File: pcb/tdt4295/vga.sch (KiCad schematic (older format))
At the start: 33 parts

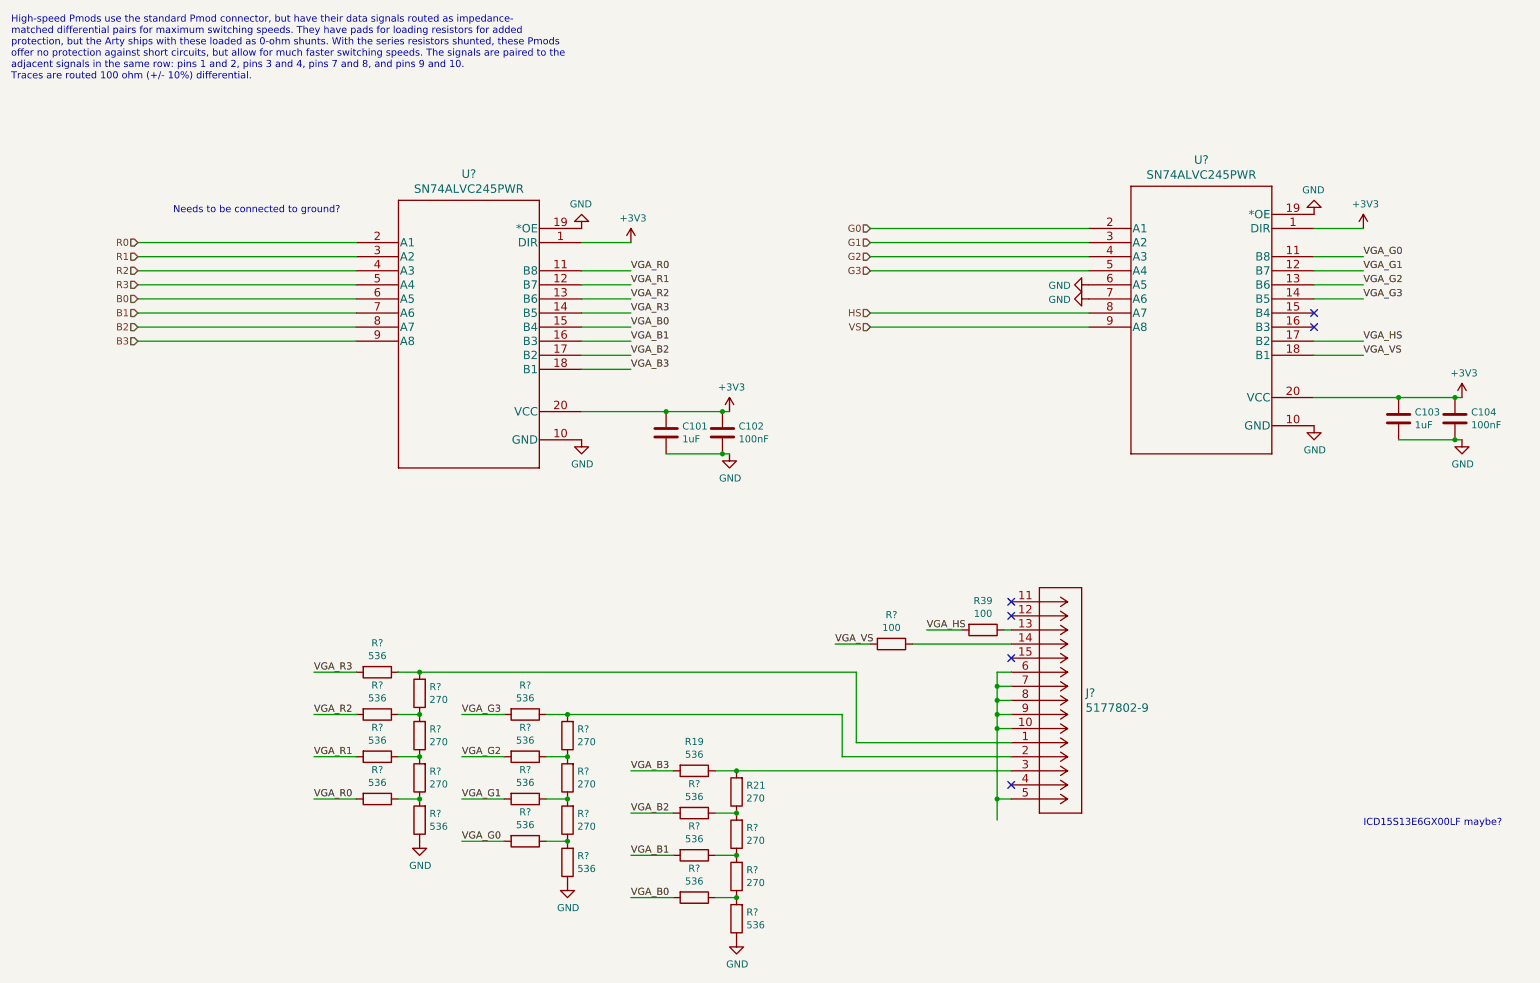
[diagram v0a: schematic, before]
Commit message: fpga external pin headers
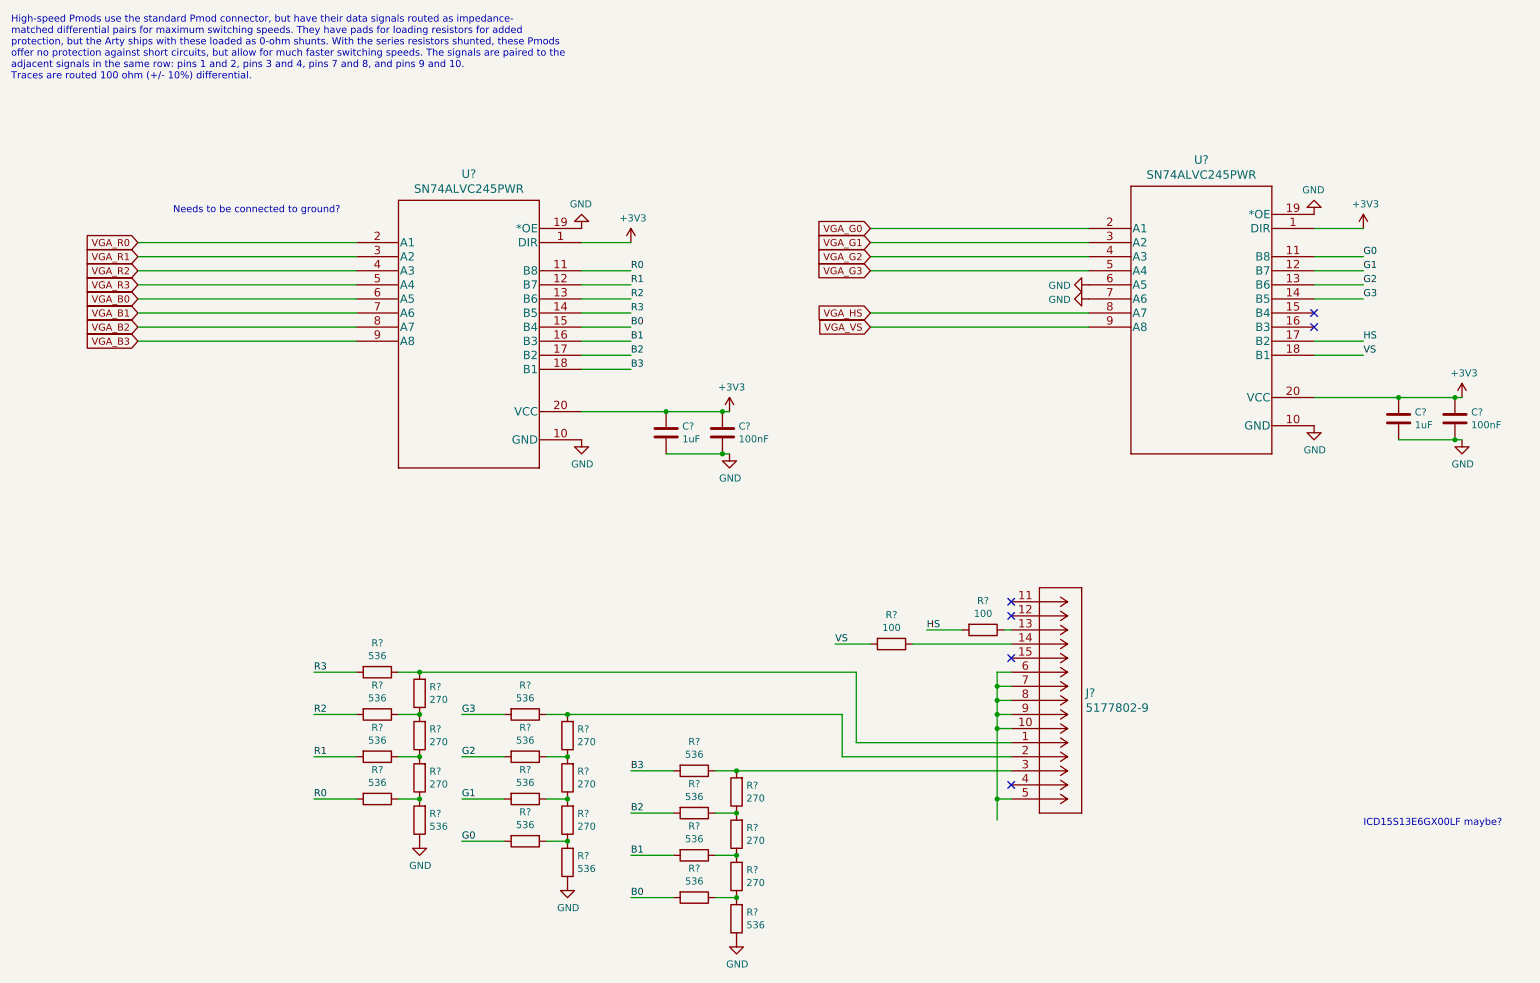
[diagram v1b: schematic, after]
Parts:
- renumbered C101 to C?, C102 to C?, C103 to C?, C104 to C?, R39 to R?, R19 to R?, R21 to R?
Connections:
- net B0: now also R?.2, U?.15 (B4); no longer U?.6 (A5)
- net B1: now also R?.2, U?.16 (B3); no longer U?.7 (A6)
- net B2: now also R?.2, U?.17 (B2); no longer U?.8 (A7)
- net B3: now also R?.2, U?.18 (B1); no longer U?.9 (A8)
- net G0: now also R?.2, U?.11 (B8); no longer U?.2 (A1)
- net G1: now also R?.2, U?.12 (B7); no longer U?.3 (A2)
- net G2: now also R?.2, U?.13 (B6); no longer U?.4 (A3)
- net G3: now also R?.2, U?.14 (B5); no longer U?.5 (A4)
- net HS: now also R?.2, U?.17 (B2); no longer U?.8 (A7)
- net R0: now also R?.2, U?.11 (B8); no longer U?.2 (A1)
- net R1: now also R?.2, U?.12 (B7); no longer U?.3 (A2)
- net R2: now also R?.2, U?.13 (B6); no longer U?.4 (A3)
- net R3: now also R?.2, U?.14 (B5); no longer U?.5 (A4)
- net VGA_B0: now also U?.6 (A5); no longer R?.2, U?.15 (B4)
- net VGA_B1: now also U?.7 (A6); no longer R?.2, U?.16 (B3)
- net VGA_B2: now also U?.8 (A7); no longer R?.2, U?.17 (B2)
- net VGA_B3: now also U?.9 (A8); no longer R?.2, U?.18 (B1)
- net VGA_G0: now also U?.2 (A1); no longer R?.2, U?.11 (B8)
- net VGA_G1: now also U?.3 (A2); no longer R?.2, U?.12 (B7)
- net VGA_G2: now also U?.4 (A3); no longer R?.2, U?.13 (B6)
- net VGA_G3: now also U?.5 (A4); no longer R?.2, U?.14 (B5)
- net VGA_HS: now also U?.8 (A7); no longer R?.2, U?.17 (B2)
- net VGA_R0: now also U?.2 (A1); no longer R?.2, U?.11 (B8)
- net VGA_R1: now also U?.3 (A2); no longer R?.2, U?.12 (B7)
- net VGA_R2: now also U?.4 (A3); no longer R?.2, U?.13 (B6)
- net VGA_R3: now also U?.5 (A4); no longer R?.2, U?.14 (B5)
- net VGA_VS: now also U?.9 (A8); no longer R?.2, U?.18 (B1)
- net VS: now also R?.2, U?.18 (B1); no longer U?.9 (A8)
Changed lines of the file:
@@
 $Descr A4 11693 8268
 encoding utf-8
-Sheet 3 3
+Sheet 4 5
 Title ""
 Date ""
@@
 	4650 3350 5250 3350
 $Comp
-L Device:C C101
+L Device:C C?
 U 1 1 61467E30
 P 5250 3500
-F 0 "C101" H 5365 3546 50  0000 L CNN
+F 0 "C?" H 5365 3546 50  0000 L CNN
 F 1 "1uF" H 5365 3455 50  0000 L CNN
 F 2 "" H 5288 3350 50  0001 C CNN
@@
 Connection ~ 5250 3350
 $Comp
-L Device:C C102
+L Device:C C?
 U 1 1 614688C2
 P 5650 3500
-F 0 "C102" H 5765 3546 50  0000 L CNN
+F 0 "C?" H 5765 3546 50  0000 L CNN
 F 1 "100nF" H 5765 3455 50  0000 L CNN
 F 2 "" H 5688 3350 50  0001 C CNN
@@
 	5250 3350 5650 3350
 Text Label 5000 2350 0    50   ~ 0
-VGA_R0
+R0
 Text Label 5000 2450 0    50   ~ 0
-VGA_R1
-Text Label 5000 2550 0    50   ~ 0
-VGA_R2
-Text Label 5000 2650 0    50   ~ 0
-VGA_R3
+R1
 Text Label 5000 2750 0    50   ~ 0
-VGA_B0
+B0
 Text Label 5000 2850 0    50   ~ 0
-VGA_B1
+B1
 Text Label 5000 2950 0    50   ~ 0
-VGA_B2
+B2
 Text Label 5000 3050 0    50   ~ 0
-VGA_B3
+B3
 Wire Wire Line
 	3050 2250 1500 2250
@@
 Wire Wire Line
 	3050 2850 1500 2850
-Text HLabel 1500 2850 0    50   Input ~ 0
-B3
-Text HLabel 1500 2750 0    50   Input ~ 0
-B2
-Text HLabel 1500 2650 0    50   Input ~ 0
-B1
-Text HLabel 1500 2550 0    50   Input ~ 0
-B0
-Text HLabel 1500 2450 0    50   Input ~ 0
-R3
-Text HLabel 1500 2350 0    50   Input ~ 0
-R2
-Text HLabel 1500 2250 0    50   Input ~ 0
-R1
-Text HLabel 1500 2150 0    50   Input ~ 0
-R0
 Text Notes 1750 1950 0    50   ~ 0
 Needs to be connected to ground?\n
@@
 	9850 3250 10450 3250
 $Comp
-L Device:C C103
+L Device:C C?
 U 1 1 61478F90
 P 10450 3400
-F 0 "C103" H 10565 3446 50  0000 L CNN
+F 0 "C?" H 10565 3446 50  0000 L CNN
 F 1 "1uF" H 10565 3355 50  0000 L CNN
 F 2 "" H 10488 3250 50  0001 C CNN
@@
 Connection ~ 10450 3250
 $Comp
-L Device:C C104
+L Device:C C?
 U 1 1 61478F97
 P 10850 3400
-F 0 "C104" H 10965 3446 50  0000 L CNN
+F 0 "C?" H 10965 3446 50  0000 L CNN
 F 1 "100nF" H 10965 3355 50  0000 L CNN
 F 2 "" H 10888 3250 50  0001 C CNN
@@
 	9850 2950 10200 2950
 Text Label 10200 2250 0    50   ~ 0
-VGA_G0
+G0
 Text Label 10200 2350 0    50   ~ 0
-VGA_G1
+G1
 Text Label 10200 2450 0    50   ~ 0
-VGA_G2
+G2
 Text Label 10200 2550 0    50   ~ 0
-VGA_G3
+G3
 Text Label 10200 2850 0    50   ~ 0
-VGA_HS
+HS
 Text Label 10200 2950 0    50   ~ 0
-VGA_VS
+VS
 NoConn ~ 9850 2650
 NoConn ~ 9850 2750
@@
 Wire Wire Line
 	8250 2350 6700 2350
-Text HLabel 6700 2350 0    50   Input ~ 0
-G3
-Text HLabel 6700 2250 0    50   Input ~ 0
-G2
-Text HLabel 6700 2150 0    50   Input ~ 0
-G1
-Text HLabel 6700 2050 0    50   Input ~ 0
-G0
 Wire Wire Line
 	8250 2650 6700 2650
 Wire Wire Line
 	8250 2750 6700 2750
-Text HLabel 6700 2750 0    50   Input ~ 0
-VS
-Text HLabel 6700 2650 0    50   Input ~ 0
-HS
 Text Notes 10200 6300 0    50   ~ 0
 ICD15S13E6GX00LF maybe?\n
@@
 	7700 4900 7650 4900
 Text Label 7100 4900 0    50   ~ 0
-VGA_HS
-$Comp
-L Device:R R39
+HS
+$Comp
+L Device:R R?
 U 1 1 6147C891
 P 7500 4900
-F 0 "R39" V 7293 4900 50  0000 C CNN
+F 0 "R?" V 7293 4900 50  0000 C CNN
 F 1 "100" V 7384 4900 50  0000 C CNN
 F 2 "" V 7430 4900 50  0001 C CNN
@@
 $EndComp
 Text Label 6450 5000 0    50   ~ 0
-VGA_VS
+VS
 Wire Wire Line
 	6450 5000 6700 5000
@@
 	7700 5900 5750 5900
 $Comp
-L Device:R R19
+L Device:R R?
 U 1 1 61490189
 P 5450 5900
-F 0 "R19" V 5243 5900 50  0000 C CNN
+F 0 "R?" V 5243 5900 50  0000 C CNN
 F 1 "536" V 5334 5900 50  0000 C CNN
 F 2 "" V 5380 5900 50  0001 C CNN
@@
 $EndComp
 $Comp
-L Device:R R21
+L Device:R R?
 U 1 1 61490B3B
 P 5750 6050
-F 0 "R21" H 5680 6004 50  0000 R CNN
+F 0 "R?" H 5680 6004 50  0000 R CNN
 F 1 "270" H 5680 6095 50  0000 R CNN
 F 2 "" V 5680 6050 50  0001 C CNN
@@
 	2750 6100 3050 6100
 Text Label 5000 5900 0    50   ~ 0
+B3
+Text Label 5000 6200 0    50   ~ 0
+B2
+Text Label 5000 6500 0    50   ~ 0
+B1
+Text Label 5000 6800 0    50   ~ 0
+B0
+Text Label 3800 6400 0    50   ~ 0
+G0
+Text Label 3800 6100 0    50   ~ 0
+G1
+Text Label 3800 5800 0    50   ~ 0
+G2
+Text Label 3800 5500 0    50   ~ 0
+G3
+Text Label 2750 6100 0    50   ~ 0
+R0
+Text Label 2750 5800 0    50   ~ 0
+R1
+Text Label 2750 5500 0    50   ~ 0
+R2
+Text Label 2750 5200 0    50   ~ 0
+R3
+Wire Wire Line
+	7700 5800 6500 5800
+Wire Wire Line
+	6500 5800 6500 5500
+Wire Wire Line
+	7700 5700 6600 5700
+Wire Wire Line
+	6600 5700 6600 5200
+Wire Wire Line
+	3500 5200 6600 5200
+Text Label 5000 2550 0    50   ~ 0
+R2
+Text Label 5000 2650 0    50   ~ 0
+R3
+Text GLabel 1500 2150 0    50   Input ~ 0
+VGA_R0
+Text GLabel 1500 2250 0    50   Input ~ 0
+VGA_R1
+Text GLabel 1500 2350 0    50   Input ~ 0
+VGA_R2
+Text GLabel 1500 2450 0    50   Input ~ 0
+VGA_R3
+Text GLabel 1500 2550 0    50   Input ~ 0
+VGA_B0
+Text GLabel 1500 2650 0    50   Input ~ 0
+VGA_B1
+Text GLabel 1500 2750 0    50   Input ~ 0
+VGA_B2
+Text GLabel 1500 2850 0    50   Input ~ 0
 VGA_B3
-Text Label 5000 6200 0    50   ~ 0
-VGA_B2
-Text Label 5000 6500 0    50   ~ 0
-VGA_B1
-Text Label 5000 6800 0    50   ~ 0
-VGA_B0
-Text Label 3800 6400 0    50   ~ 0
+Text GLabel 6700 2050 0    50   Input ~ 0
 VGA_G0
-Text Label 3800 6100 0    50   ~ 0
+Text GLabel 6700 2150 0    50   Input ~ 0
 VGA_G1
-Text Label 3800 5800 0    50   ~ 0
+Text GLabel 6700 2250 0    50   Input ~ 0
 VGA_G2
-Text Label 3800 5500 0    50   ~ 0
+Text GLabel 6700 2350 0    50   Input ~ 0
 VGA_G3
-Text Label 2750 6100 0    50   ~ 0
-VGA_R0
-Text Label 2750 5800 0    50   ~ 0
-VGA_R1
-Text Label 2750 5500 0    50   ~ 0
-VGA_R2
-Text Label 2750 5200 0    50   ~ 0
-VGA_R3
-Wire Wire Line
-	7700 5800 6500 5800
-Wire Wire Line
-	6500 5800 6500 5500
-Wire Wire Line
-	7700 5700 6600 5700
-Wire Wire Line
-	6600 5700 6600 5200
-Wire Wire Line
-	3500 5200 6600 5200
+Text GLabel 6700 2650 0    50   Input ~ 0
+VGA_HS
+Text GLabel 6700 2750 0    50   Input ~ 0
+VGA_VS
 $EndSCHEMATC

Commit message: add another capacitor :)
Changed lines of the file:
@@
 Wire Wire Line
 	8250 2750 6700 2750
-Text Notes 10200 6300 0    50   ~ 0
+Text Notes 8450 5700 0    50   ~ 0
 ICD15S13E6GX00LF maybe?\n
 $Comp
